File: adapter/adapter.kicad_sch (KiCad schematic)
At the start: 22 parts, among them J10 Ribbon, J11 Ribbon, J12 Ribbon, J13 serial, J14 serial, J3 battery charge, J6 battery charge, J7 trackball, J8 trackball, J9 Ribbon, SW1 SW_SPST, SW2 SW_SPST, SW3 SW_SPDT, SW4 SW_SPDT, U1 eliteC, U2 eliteC

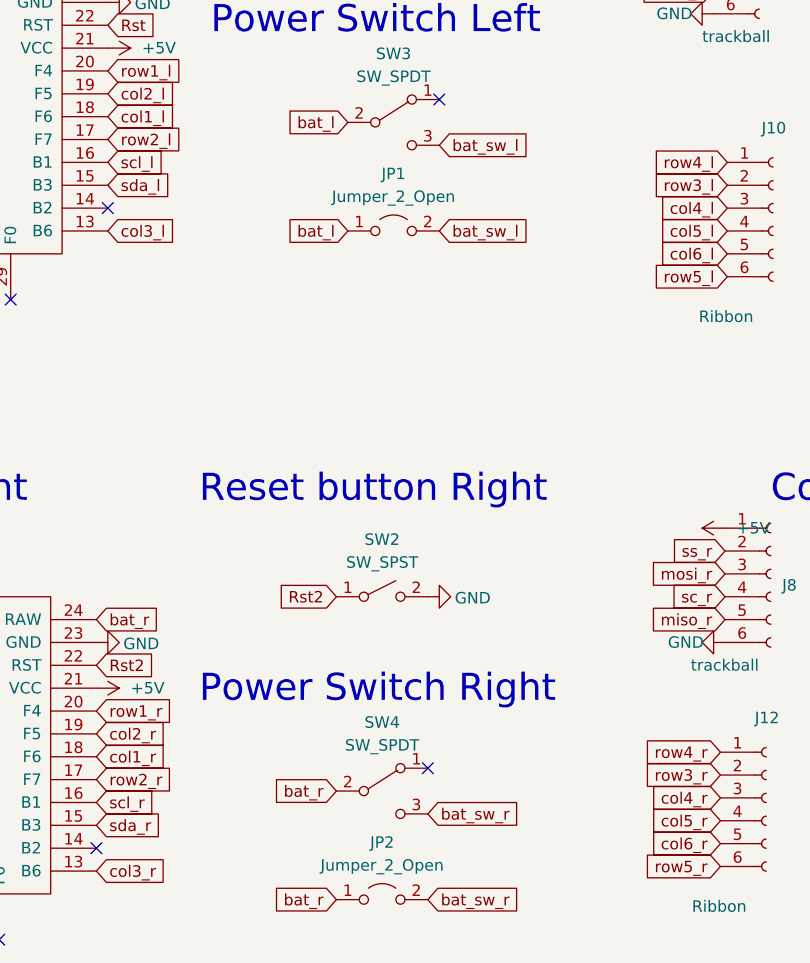
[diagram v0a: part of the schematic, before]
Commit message: v0.2
removed serial ports
moved reset to be reachable
replace on/off switch to top and swapped to vertical through hole
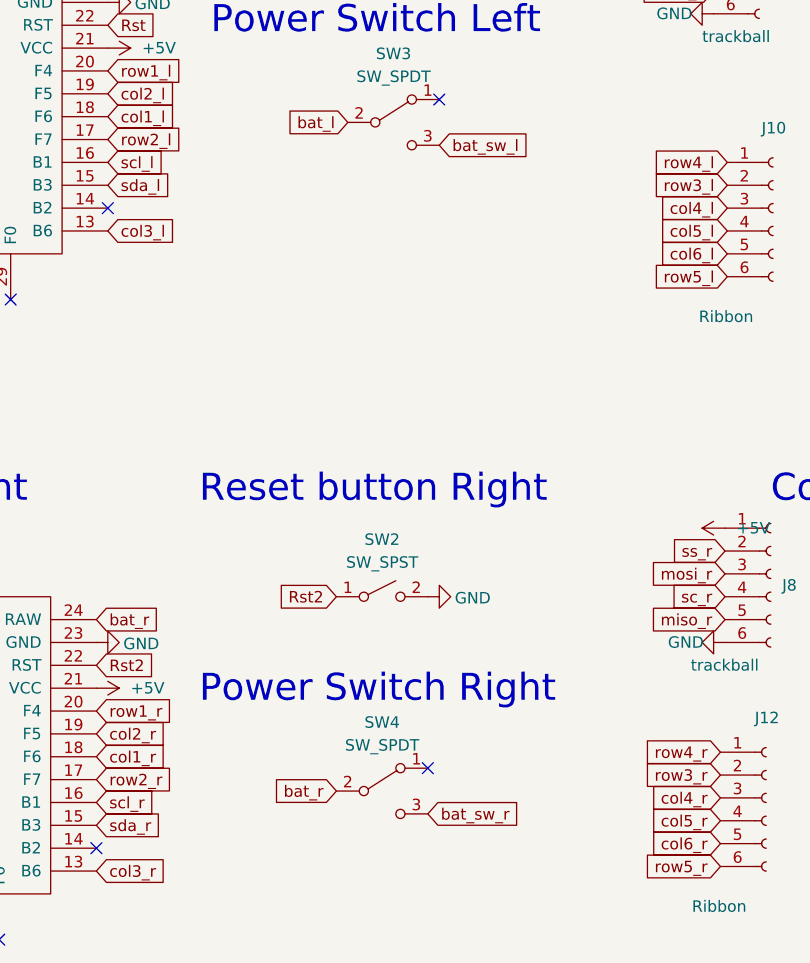
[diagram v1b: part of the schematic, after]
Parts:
- removed JP1, JP2: Jumper_2_Open, Library:power_switch_jumper, symbol Jumper:Jumper_2_Open
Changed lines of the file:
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@@
-    )
-  )
-  (global_label "bat_l" (shape input) (at 91.44 69.85 180)
-    (effects (font (size 1.27 1.27)) (justify right))
-    (property "Intersheetrefs" "${INTERSHEET_REFS}" (at 214.63 200.66 0)
-      (effects (font (size 1.27 1.27)) hide)
     )
   )
@@
     )
   )
-  (global_label "bat_sw_r" (shape input) (at 100.33 144.145 0)
-    (effects (font (size 1.27 1.27)) (justify left))
-    (property "Intersheetrefs" "${INTERSHEET_REFS}" (at -22.86 13.335 0)
-      (effects (font (size 1.27 1.27)) hide)
-    )
-  )
   (global_label "row1_l" (shape input) (at 172.974 35.56 180)
     (effects (font (size 1.27 1.27)) (justify right))
@@
     )
   )
-  (global_label "bat_r" (shape input) (at 90.17 144.145 180)
-    (effects (font (size 1.27 1.27)) (justify right))
-    (property "Intersheetrefs" "${INTERSHEET_REFS}" (at 213.36 274.955 0)
-      (effects (font (size 1.27 1.27)) hide)
-    )
-  )
   (global_label "row3_l" (shape input) (at 133.604 64.77 180)
     (effects (font (size 1.27 1.27)) (justify right))
@@
     (effects (font (size 1.27 1.27)) (justify right))
     (property "Intersheetrefs" "${INTERSHEET_REFS}" (at 147.32 64.516 0)
-      (effects (font (size 1.27 1.27)) hide)
-    )
-  )
-  (global_label "bat_sw_l" (shape input) (at 101.6 69.85 0)
-    (effects (font (size 1.27 1.27)) (justify left))
-    (property "Intersheetrefs" "${INTERSHEET_REFS}" (at -21.59 -60.96 0)
       (effects (font (size 1.27 1.27)) hide)
     )
@@
     )
   )
-  (symbol (lib_id "Jumper:Jumper_2_Open") (at 95.25 144.145 0) (unit 1)
-    (in_bom yes) (on_board yes) (dnp no) (fields_autoplaced)
-    (property "Reference" "JP2" (at 95.25 137.795 0)
-      (effects (font (size 1.27 1.27)))
-    )
-    (property "Value" "Jumper_2_Open" (at 95.25 140.335 0)
-      (effects (font (size 1.27 1.27)))
-    )
-    (property "Footprint" "Library:power_switch_jumper" (at 95.25 144.145 0)
-      (effects (font (size 1.27 1.27)) hide)
-    )
-    (property "Datasheet" "~" (at 95.25 144.145 0)
-      (effects (font (size 1.27 1.27)) hide)
-    )
-    (pin "1")
-    (pin "2")
-    (instances
-      (project "adapter"
-        (path "/e63e39d7-6ac0-4ffd-8aa3-1841a4541b55"
-          (reference "JP2") (unit 1)
-        )
-      )
-    )
-  )
   (symbol (lib_id "Switch:SW_SPDT") (at 96.52 57.785 0) (unit 1)
     (in_bom yes) (on_board yes) (dnp no) (fields_autoplaced)
@@
         )
       )
-    )
-  )
-  (symbol (lib_id "Jumper:Jumper_2_Open") (at 96.52 69.85 0) (unit 1)
-    (in_bom yes) (on_board yes) (dnp no) (fields_autoplaced)
-    (property "Reference" "JP1" (at 96.52 63.5 0)
-      (effects (font (size 1.27 1.27)))
-    )
-    (property "Value" "Jumper_2_Open" (at 96.52 66.04 0)
-      (effects (font (size 1.27 1.27)))
-    )
-    (property "Footprint" "Library:power_switch_jumper" (at 96.52 69.85 0)
-      (effects (font (size 1.27 1.27)) hide)
-    )
-    (property "Datasheet" "~" (at 96.52 69.85 0)
-      (effects (font (size 1.27 1.27)) hide)
-    )
-    (pin "1")
-    (pin "2")
-    (instances
-      (project "adapter"
-        (path "/e63e39d7-6ac0-4ffd-8aa3-1841a4541b55"
-          (reference "JP1") (unit 1)
-        )
-      )
